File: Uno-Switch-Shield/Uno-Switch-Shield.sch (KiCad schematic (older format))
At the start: 30 parts, among them P1 Power, P10 CONN_01X10, P11 CONN_01X10, P12 CONN_01X10, P2 Analog, P3 Digital, P4 Digital, P5 CONN_01X01, P6 CONN_01X01, P7 CONN_01X01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

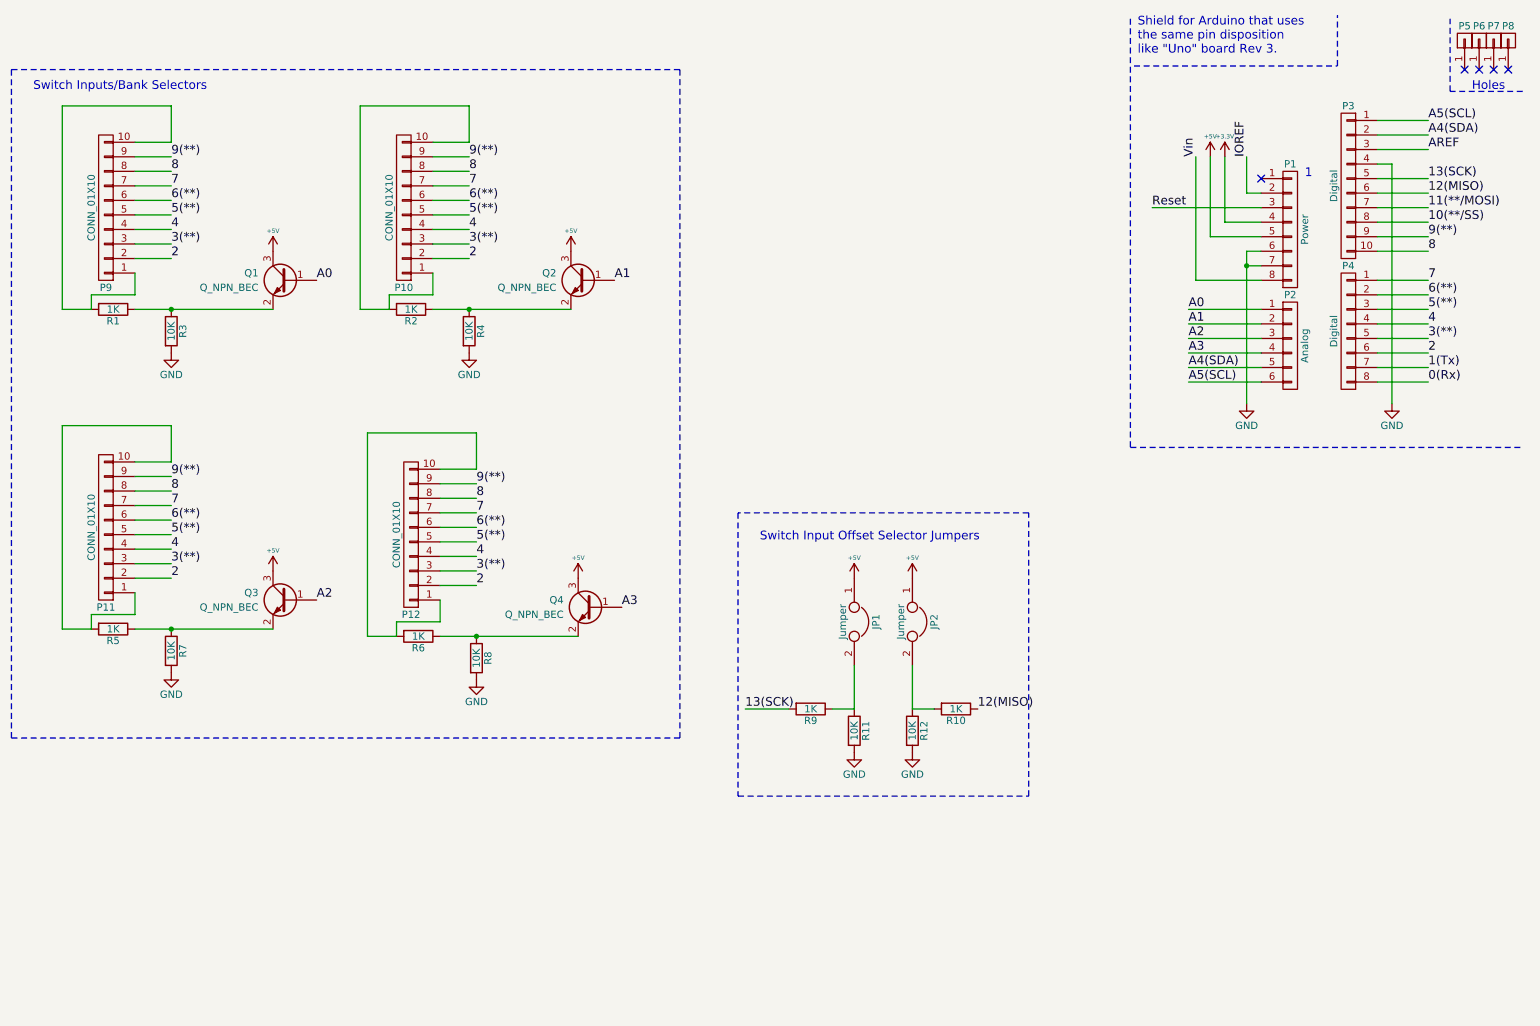
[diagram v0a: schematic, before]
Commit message: Made the Uno Switch Shield six headers instead of four. Also some re-exporting of gerbers.
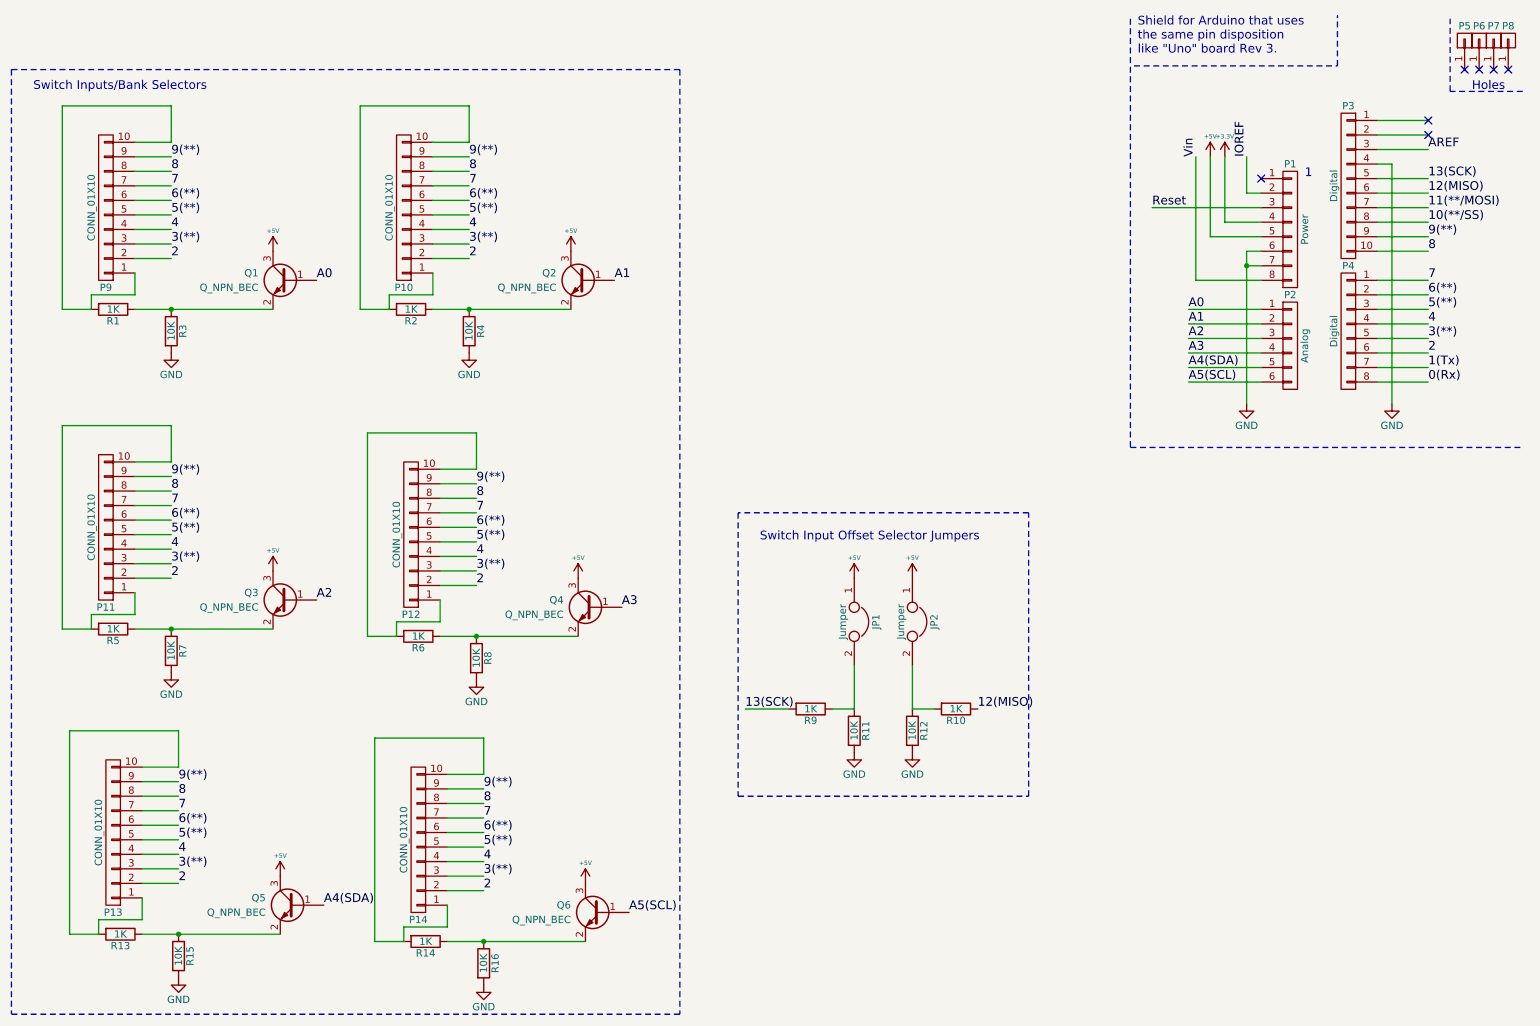
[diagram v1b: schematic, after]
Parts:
- added P13, P14: CONN_01X10, Socket_Strips:Socket_Strip_Straight_1x10_Pitch2.54mm, symbol CONN_01X10
- added Q5, Q6: Q_NPN_BEC, TO_SOT_Packages_SMD:SOT-23, symbol Q_NPN_BEC
- added R13, R14: 1K, Resistors_SMD:R_0805, symbol R
- added R15, R16: 10K, Resistors_SMD:R_0805, symbol R
- P10, P11, P12, P9: footprint Socket_Strips:Socket_Strip_Straight_1x10 -> Socket_Strips:Socket_Strip_Straight_1x10_Pitch2.54mm
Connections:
- net +5V: now also Q5.3 (C), Q6.3 (C)
- net 2: now also P13.2 (P2), P14.2 (P2)
- net 3(**): now also P13.3 (P3), P14.3 (P3)
- net 4: now also P13.4 (P4), P14.4 (P4)
- net 5(**): now also P13.5 (P5), P14.5 (P5)
- net 6(**): now also P13.6 (P6), P14.6 (P6)
- net 7: now also P13.7 (P7), P14.7 (P7)
- net 8: now also P13.8 (P8), P14.8 (P8)
- net 9(**): now also P13.9 (P9), P14.9 (P9)
- net A4(SDA): now also Q5.1 (B); no longer P3.2 (P2)
- net A5(SCL): now also Q6.1 (B); no longer P3.1 (P1)
- net GND: now also R15.2, R16.2
- new net: P13.1 (P1), P13.10 (P10), R13.2
- new net: Q5.2 (E), R13.1, R15.1
- new net: P14.1 (P1), P14.10 (P10), R14.2
- new net: Q6.2 (E), R14.1, R16.1
- no-connect marks 5 -> 7
